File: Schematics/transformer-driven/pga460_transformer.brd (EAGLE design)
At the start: 112.5 x 66.7 mm, 59 parts, among them T1 B78416A2232A003, T2 B78416A2232A003, T3 B78416A2232A003, U1 PGA460, U2 PGA460, U4 PGA460

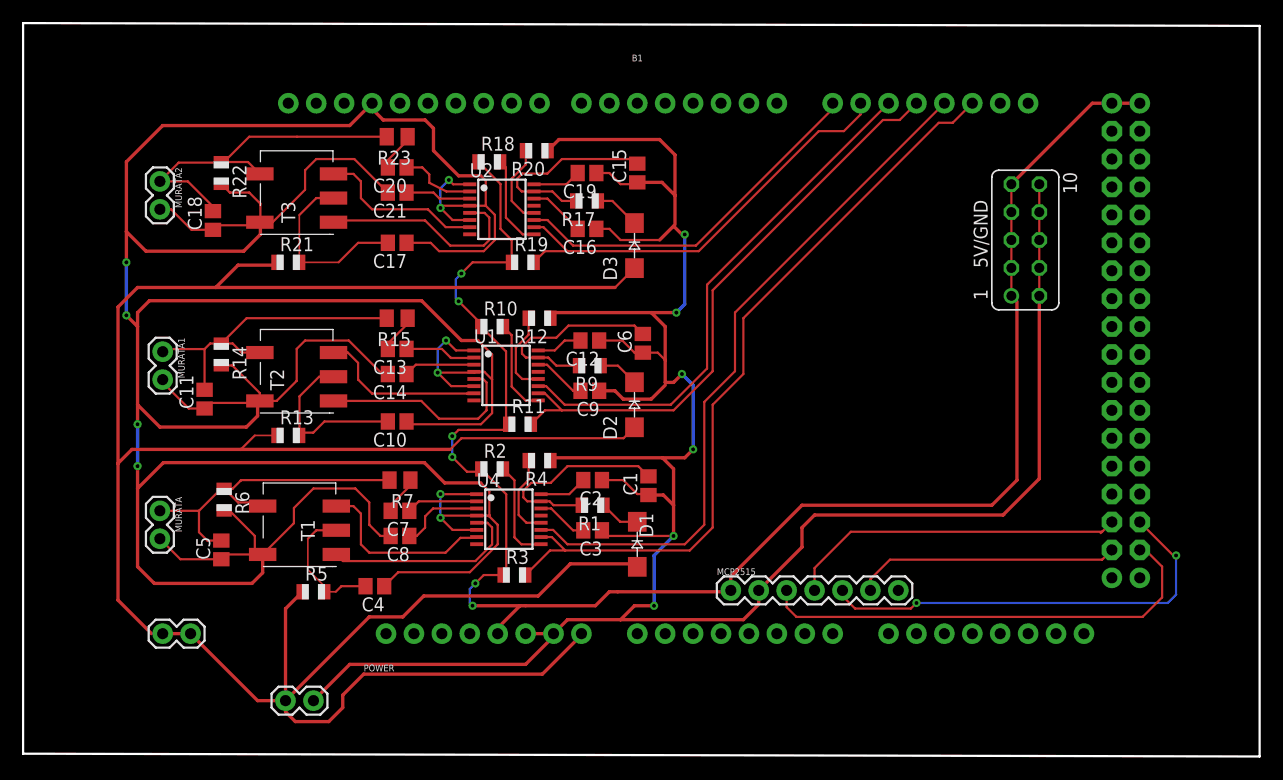
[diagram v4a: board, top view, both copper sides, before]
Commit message: Revert "change pga460"
This reverts commit 11281d79b47b0006704001165f10d30d9cd033b8
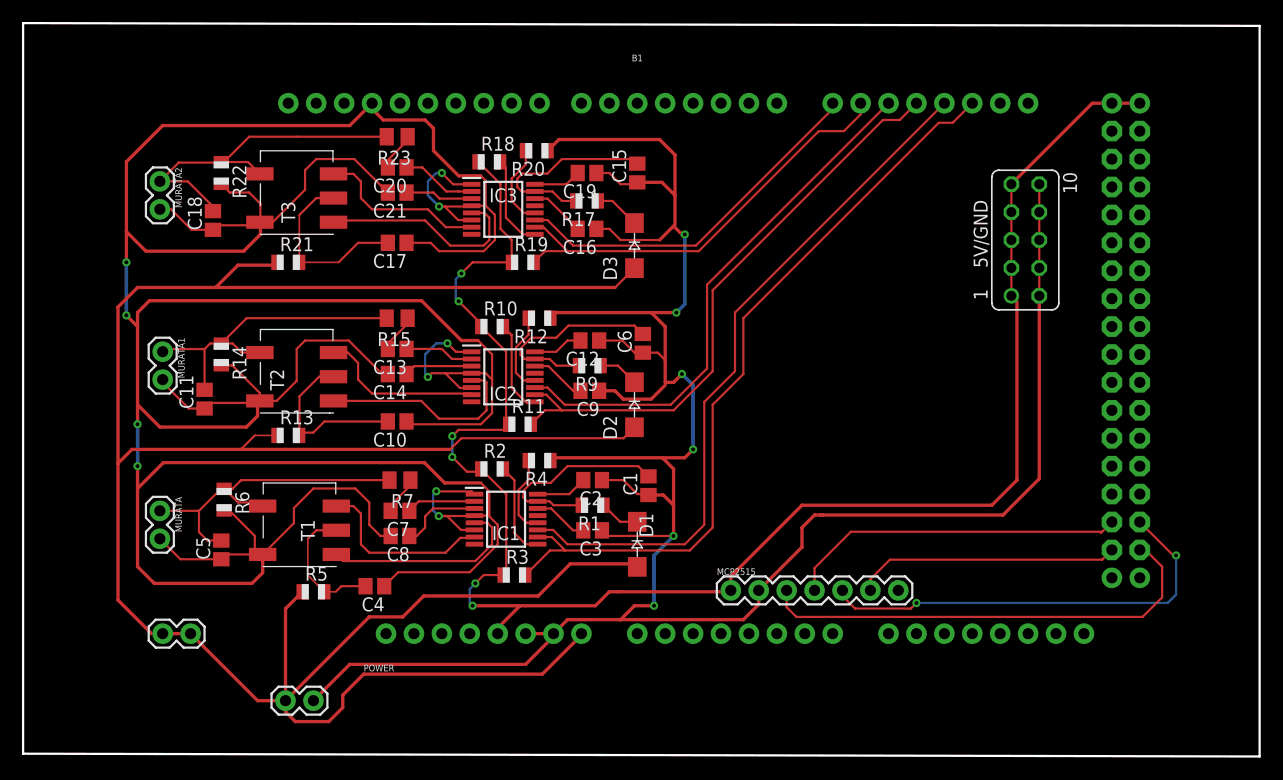
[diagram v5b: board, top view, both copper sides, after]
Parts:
- removed U1, U2, U4: PGA460, texas:TSSOP16
- added IC1, IC2, IC3: PGA460TPWQ1, PGA460TPWQ1:SOP65P640X120-16N
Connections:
- net AVDD1: now also IC1.16; no longer U4.16
- net AVDD2: now also IC2.16; no longer U1.16
- net AVDD3: now also IC3.16; no longer U2.16
- net GND: now also IC1.1, IC1.4, IC1.6, IC2.1, IC2.4, IC2.6, IC3.1, IC3.4, IC3.6; no longer U1.1, U1.4, U1.6, U2.1, U2.4, U2.6, U4.1, U4.4, U4.6
- net INN_1: now also IC1.3; no longer U4.3
- net INN_2: now also IC2.3; no longer U1.3
- net INN_3: now also IC3.3; no longer U2.3
- net INP_1: now also IC1.2; no longer U4.2
- net INP_2: now also IC2.2; no longer U1.2
- net INP_3: now also IC3.2; no longer U2.2
- net IOREG1: now also IC1.14; no longer U4.14
- net IOREG2: now also IC2.14; no longer U1.14
- net IOREG3: now also IC3.14; no longer U2.14
- net OUTA_1: now also IC1.5; no longer U4.5
- net OUTA_2: now also IC2.5; no longer U1.5
- net OUTA_3: now also IC3.5; no longer U2.5
- net OUTB_1: now also IC1.7; no longer U4.7
- net OUTB_2: now also IC2.7; no longer U1.7
- net OUTB_3: now also IC3.7; no longer U2.7
- net RX1: now also IC1.10; no longer U4.10
- net RX2: now also IC2.10; no longer U1.10
- net RX3: now also IC3.10; no longer U2.10
- net SCLK1: now also IC1.12; no longer U4.12
- net SCLK2: now also IC2.12; no longer U1.12
- net SCLK3: now also IC3.12; no longer U2.12
- net TEST1: now also IC1.9
- net TEST2: now also IC2.9
- net TEST3: now also IC3.9
- net TX1: now also IC1.11; no longer U4.11
- net TX2: now also IC2.11; no longer U1.11
- net TX3: now also IC3.11; no longer U2.11
- net VIN: now also IC1.15, IC2.15, IC3.15; no longer U1.15, U2.15, U4.15
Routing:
- net GND: track 612.9 -> 617.3 mm
- net N$2: track 1.40 -> 0.00 mm
- net N$1: track 1.27 -> 0.00 mm
- net TEST3: track 7.44 -> 8.54 mm
- net TEST2: track 7.56 -> 8.54 mm
- net TEST1: track 9.58 -> 8.80 mm

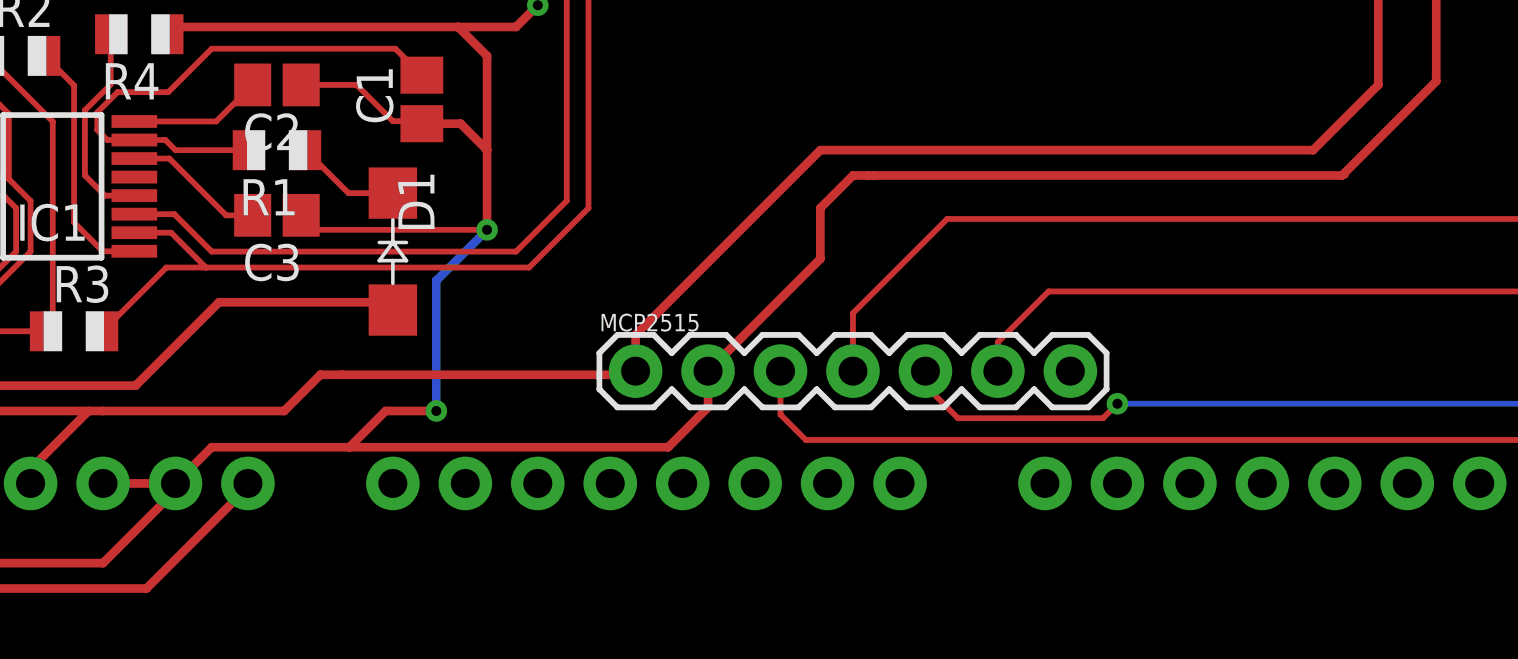
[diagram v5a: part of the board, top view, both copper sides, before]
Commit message: move track to avoid crossing
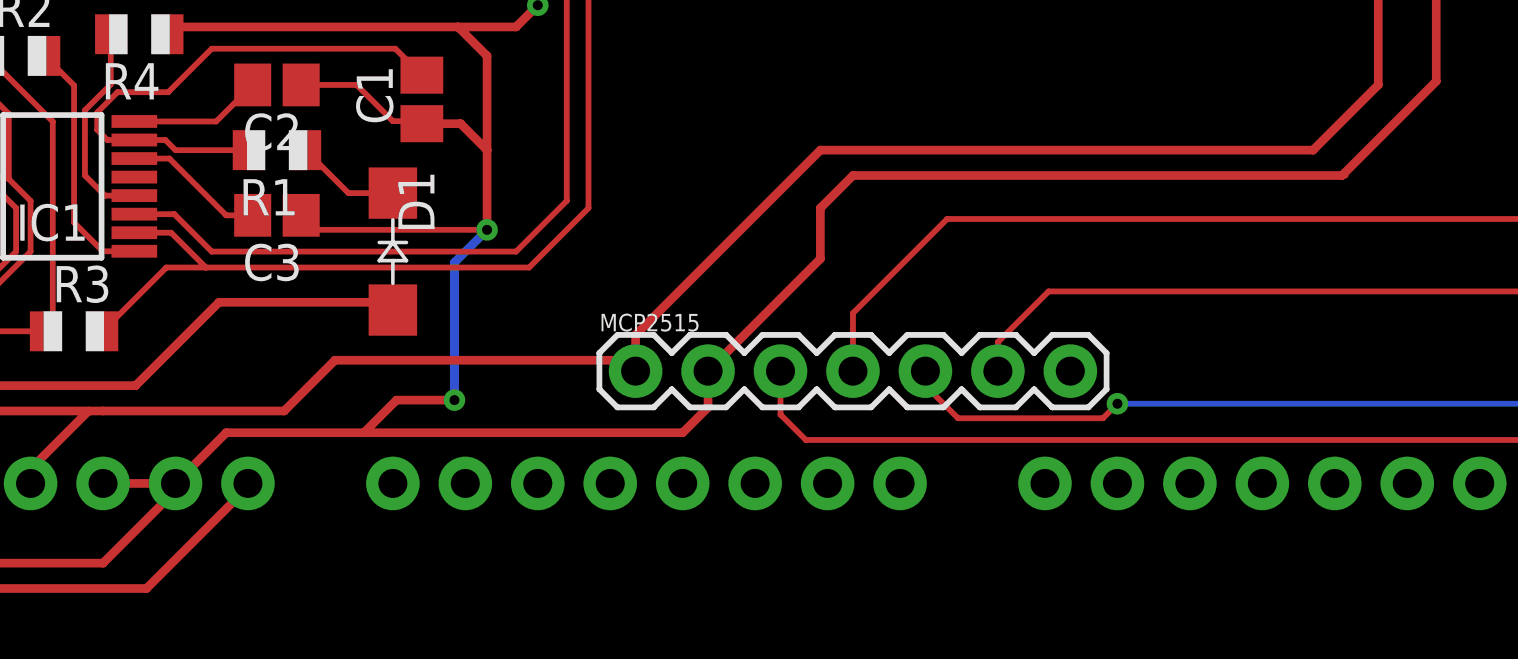
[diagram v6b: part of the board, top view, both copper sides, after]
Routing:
- net GND: track 617.3 -> 616.7 mm
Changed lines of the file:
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@@
 <drawing>
 <settings>
-<setting alwaysvectorfont="yes"/>
+<setting alwaysvectorfont="no"/>
 <setting verticaltext="up"/>
 </settings>
@@
 <wire x1="52.666" y1="-41.656" x2="52.816" y2="-41.506" width="0.2032" layer="1"/>
 <wire x1="52.666" y1="-46.228" x2="53.174" y2="-46.736" width="0.2032" layer="1"/>
-<wire x1="49.53" y1="-54.356" x2="48.26" y2="-55.626" width="0.3048" layer="1"/>
+<wire x1="50.038" y1="-53.848" x2="48.26" y2="-55.626" width="0.3048" layer="1"/>
 <wire x1="41.067" y1="-44.887" x2="40.64" y2="-44.887" width="0.2032" layer="1"/>
 <wire x1="40.64" y1="-44.887" x2="40.386" y2="-44.887" width="0.2032" layer="1"/>
 <wire x1="39.837" y1="-46.187" x2="41.067" y2="-46.187" width="0.2032" layer="1"/>
-<wire x1="65.532" y1="-54.356" x2="54.356" y2="-54.356" width="0.3048" layer="1"/>
-<wire x1="54.356" y1="-54.356" x2="49.53" y2="-54.356" width="0.3048" layer="1"/>
+<wire x1="66.04" y1="-53.848" x2="54.864" y2="-53.848" width="0.3048" layer="1"/>
+<wire x1="54.864" y1="-53.848" x2="50.038" y2="-53.848" width="0.3048" layer="1"/>
 <wire x1="47.99" y1="-26.924" x2="48.498" y2="-26.416" width="0.2032" layer="1"/>
 <wire x1="57.15" y1="-26.416" x2="48.498" y2="-26.416" width="0.3048" layer="1"/>
@@
 <wire x1="31.75" y1="-7.874" x2="31.75" y2="-7.366" width="0.3048" layer="1"/>
 <wire x1="45.72" y1="-55.626" x2="48.26" y2="-55.626" width="0.3048" layer="1"/>
-<wire x1="72.517" y1="-44.831" x2="72.771" y2="-44.831" width="0.3048" layer="1"/>
-<wire x1="72.771" y1="-44.831" x2="89.154" y2="-44.831" width="0.3048" layer="1"/>
+<wire x1="72.009" y1="-44.831" x2="89.154" y2="-44.831" width="0.3048" layer="1"/>
 <wire x1="89.154" y1="-44.831" x2="89.281" y2="-44.831" width="0.2032" layer="1"/>
 <wire x1="34.886" y1="-20.066" x2="37.084" y2="-20.066" width="0.2032" layer="1"/>
@@
 <wire x1="9.398" y1="-19.05" x2="11.176" y2="-20.828" width="0.3048" layer="1"/>
 <wire x1="11.176" y1="-20.828" x2="20.066" y2="-20.828" width="0.3048" layer="1"/>
-<wire x1="54.356" y1="-54.356" x2="55.626" y2="-53.086" width="0.3048" layer="1"/>
-<wire x1="55.626" y1="-53.086" x2="57.404" y2="-53.086" width="0.3048" layer="1"/>
-<via x="57.404" y="-53.086" extent="1-16" drill="0.35"/>
-<wire x1="57.404" y1="-53.086" x2="57.404" y2="-48.514" width="0.3048" layer="16"/>
-<wire x1="57.404" y1="-48.514" x2="59.182" y2="-46.736" width="0.3048" layer="16"/>
+<wire x1="54.864" y1="-53.848" x2="56.007" y2="-52.705" width="0.3048" layer="1"/>
+<wire x1="56.007" y1="-52.705" x2="58.039" y2="-52.705" width="0.3048" layer="1"/>
+<via x="58.039" y="-52.705" extent="1-16" drill="0.35"/>
+<wire x1="58.039" y1="-52.705" x2="58.039" y2="-47.879" width="0.3048" layer="16"/>
+<wire x1="58.039" y1="-47.879" x2="59.182" y2="-46.736" width="0.3048" layer="16"/>
 <via x="59.182" y="-46.736" extent="1-16" drill="0.35"/>
 <wire x1="42.093" y1="-16.693" x2="42.926" y2="-17.526" width="0.2032" layer="1"/>
@@
 <contactref element="MCP2515" pad="2"/>
 <wire x1="66.929" y1="-52.959" x2="66.929" y2="-51.689" width="0.3048" layer="1"/>
-<wire x1="65.532" y1="-54.356" x2="66.929" y2="-52.959" width="0.3048" layer="1"/>
+<wire x1="66.04" y1="-53.848" x2="66.929" y2="-52.959" width="0.3048" layer="1"/>
 <wire x1="66.929" y1="-51.689" x2="70.866" y2="-47.752" width="0.3048" layer="1"/>
 <wire x1="70.866" y1="-47.752" x2="70.866" y2="-45.974" width="0.3048" layer="1"/>
 <wire x1="70.866" y1="-45.974" x2="72.009" y2="-44.831" width="0.3048" layer="1"/>
-<wire x1="72.009" y1="-44.831" x2="72.517" y2="-44.831" width="0.3048" layer="1"/>
 <wire x1="22.7" y1="-18.194" x2="22.606" y2="-18.542" width="0" layer="19" extent="1-1"/>
 </signal>
@@
 <contactref element="B1" pad="5V@2"/>
 <contactref element="B1" pad="5V"/>
-<wire x1="54.626" y1="-51.816" x2="54.102" y2="-51.816" width="0.2032" layer="1"/>
-<wire x1="53.34" y1="-51.816" x2="54.102" y2="-51.816" width="0.3048" layer="1"/>
-<wire x1="53.34" y1="-51.816" x2="52.07" y2="-53.086" width="0.3048" layer="1"/>
+<wire x1="53.848" y1="-51.308" x2="64.008" y2="-51.308" width="0.3048" layer="1"/>
+<wire x1="53.848" y1="-51.308" x2="52.07" y2="-53.086" width="0.3048" layer="1"/>
 <wire x1="52.07" y1="-53.086" x2="45.72" y2="-53.086" width="0.3048" layer="1"/>
 <wire x1="45.72" y1="-53.086" x2="45.212" y2="-53.086" width="0.2032" layer="1"/>
@@
 <wire x1="40.894" y1="-53.086" x2="45.72" y2="-53.086" width="0.3048" layer="1"/>
 <contactref element="MCP2515" pad="1"/>
-<wire x1="64.262" y1="-51.816" x2="64.389" y2="-51.689" width="0.3048" layer="1"/>
-<wire x1="54.102" y1="-51.816" x2="64.262" y2="-51.816" width="0.3048" layer="1"/>
+<wire x1="64.389" y1="-51.689" x2="64.008" y2="-51.308" width="0.3048" layer="1"/>
 <wire x1="70.866" y1="-43.942" x2="64.389" y2="-50.419" width="0.3048" layer="1"/>
 <wire x1="64.389" y1="-50.419" x2="64.389" y2="-51.689" width="0.3048" layer="1"/>

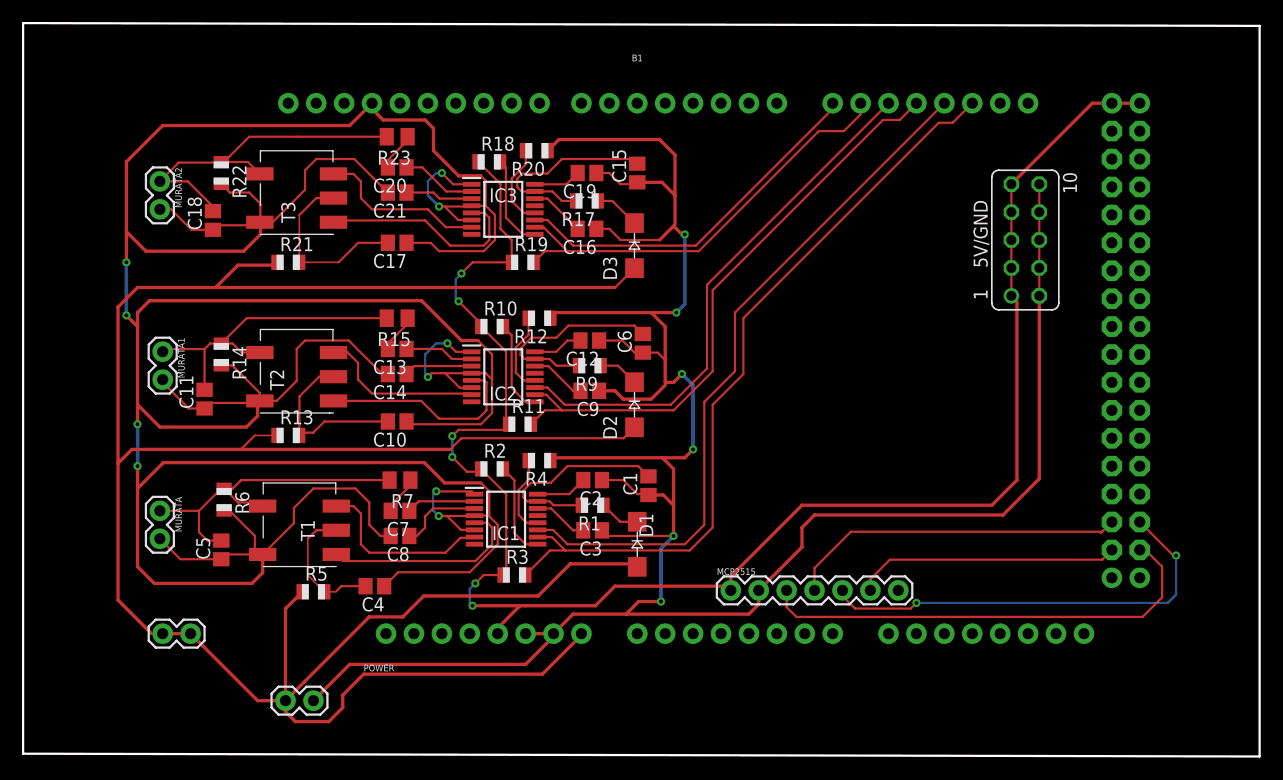
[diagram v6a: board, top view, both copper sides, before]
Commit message: Prevent smaller gaps between tracks
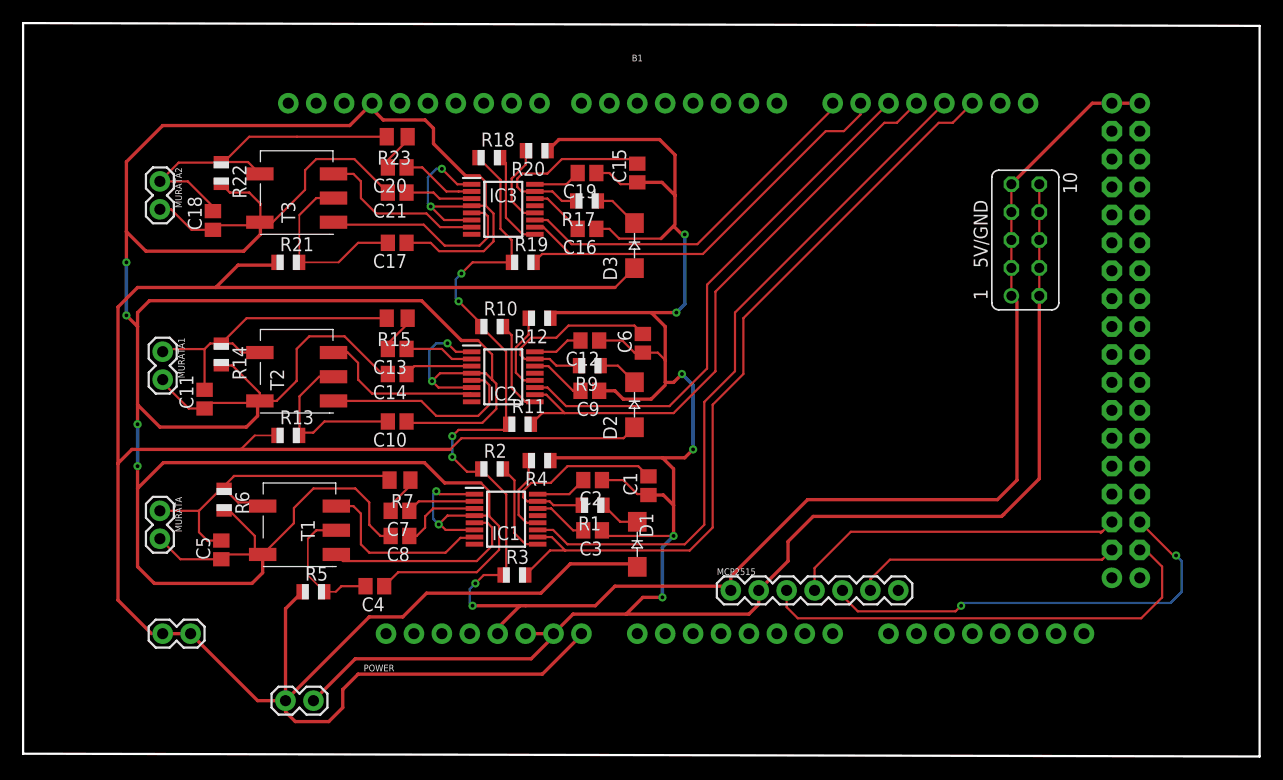
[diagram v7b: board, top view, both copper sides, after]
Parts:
- moved R18 0.38 mm to (42.4, -12.3)
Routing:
- net GND: track 616.7 -> 620.6 mm
- net MOSI: track 40.2 -> 41.0 mm
